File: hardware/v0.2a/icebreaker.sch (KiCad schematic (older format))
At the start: 108 parts, among them J1 Jumper, J10 Jumper, J11 Jumper, J12 Jumper, J13 Jumper, J14 Jumper, J15 Jumper, J16 Jumper, J17 Jumper, J18 Jumper, J19 Jumper, J2 Jumper, J20 Flash, J21 PMOD_1A, J22 PMOD_1B, J23 PMOD_2H, J24 PMOD_2P, J25 RGB Led, J26 5V AUX, J27 5V AUX, J3 Jumper, J4 Jumper, J5 Jumper, J6 Jumper, J7 Jumper, J8 Jumper, J9 Jumper, P1 pkl_USB_OTG, SW1 TACT, SW2 TACT, SW3 TACT, SW4 TACT, U1 93C46B-SOT-23-6, U2 3.3V, U3 1V2, U4 FT2232H, U5 W25Q, U6 ICE5LP4K-SG48, X1 12MHz

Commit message: Fixed #6 Oscillator pinout and schematic symbol.
Both bitsy and icebreaker.
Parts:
- removed X1: 12MHz, pkl_housings_sot:SOT-23-5, symbol pkl_device:Oscillator
- added U7: 12MHz, pkl_housings_sot:SOT-23-5, symbol pkl_device:pkl_oscillator_sit2001
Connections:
- wire segments 585 -> 581
- no-connect marks 17 -> 18
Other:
- moved on the sheet: C4, R7
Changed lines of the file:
@@
 $EndComp
 $Comp
-L pkl_device:Oscillator X1
-U 1 1 5A523EA3
-P 1900 6750
-F 0 "X1" H 1900 6355 60  0000 C CNN
-F 1 "12MHz" H 1900 6465 60  0000 C CNN
-F 2 "pkl_housings_sot:SOT-23-5" H 1900 6750 60  0001 C CNN
-F 3 "https://www.sitime.com/datasheet/SiT2001" H 1900 6750 60  0001 C CNN
-F 4 "12MHz Oscillator" H 1900 6750 50  0001 C CNN "Description"
-F 5 "SiTIME" H 1900 6750 50  0001 C CNN "Manufacturer"
-F 6 "SIT2001BI-S2-33E-12.000000G" H 1900 6750 50  0001 C CNN "MFN"
-F 7 "ANY" H 1900 6750 50  0001 C CNN "Source"
-F 8 "xtal-sot23-5-12mhz-osc" H 0   0   50  0001 C CNN "Key"
-	1    1900 6750
-	-1   0    0    1
-$EndComp
-Wire Wire Line
-	2300 6750 2400 6750
-$Comp
 L pkl_device:pkl_R_Small R7
 U 1 1 5A52417F
-P 2500 6750
-F 0 "R7" V 2550 6900 50  0000 C CNN
-F 1 "10k" V 2550 6600 50  0000 C CNN
-F 2 "pkl_dipol:R_0402" H 2559 6657 60  0001 L CNN
-F 3 "" H 2500 6750 60  0000 C CNN
-F 4 "ANY" H 2500 6750 50  0001 C CNN "Source"
-F 5 "res-0402-10k" H 0   0   50  0001 C CNN "Key"
-	1    2500 6750
-	0    1    1    0
+P 1300 6700
+F 0 "R7" V 1350 6850 50  0000 C CNN
+F 1 "10k" V 1350 6550 50  0000 C CNN
+F 2 "pkl_dipol:R_0402" H 1359 6607 60  0001 L CNN
+F 3 "" H 1300 6700 60  0000 C CNN
+F 4 "ANY" H 1300 6700 50  0001 C CNN "Source"
+F 5 "res-0402-10k" H -1200 -50 50  0001 C CNN "Key"
+	1    1300 6700
+	0    -1   -1   0
 $EndComp
 $Comp
 L power:+3V3 #PWR02
 U 1 1 5A524395
-P 2800 6550
-F 0 "#PWR02" H 2800 6400 50  0001 C CNN
-F 1 "+3V3" H 2815 6726 50  0000 C CNN
-F 2 "" H 2800 6550 50  0001 C CNN
-F 3 "" H 2800 6550 50  0001 C CNN
-	1    2800 6550
+P 1100 6600
+F 0 "#PWR02" H 1100 6450 50  0001 C CNN
+F 1 "+3V3" H 1115 6776 50  0000 C CNN
+F 2 "" H 1100 6600 50  0001 C CNN
+F 3 "" H 1100 6600 50  0001 C CNN
+	1    1100 6600
 	1    0    0    -1
 $EndComp
-Wire Wire Line
-	1500 6650 1400 6650
-Wire Wire Line
-	1400 6650 1400 6550
 $Comp
 L power:+3V3 #PWR03
 U 1 1 5A5243FF
-P 1400 6550
-F 0 "#PWR03" H 1400 6400 50  0001 C CNN
-F 1 "+3V3" H 1415 6726 50  0000 C CNN
-F 2 "" H 1400 6550 50  0001 C CNN
-F 3 "" H 1400 6550 50  0001 C CNN
-	1    1400 6550
+P 2600 6600
+F 0 "#PWR03" H 2600 6450 50  0001 C CNN
+F 1 "+3V3" H 2615 6776 50  0000 C CNN
+F 2 "" H 2600 6600 50  0001 C CNN
+F 3 "" H 2600 6600 50  0001 C CNN
+	1    2600 6600
 	1    0    0    -1
 $EndComp
-Wire Wire Line
-	1500 6750 1400 6750
-Wire Wire Line
-	1400 6750 1400 7050
 NoConn ~ 3100 6750
 Wire Wire Line
@@
 L pkl_device:pkl_C_Small C4
 U 1 1 5A526171
-P 1200 6850
-F 0 "C4" H 1292 6897 50  0000 L CNN
-F 1 "100n" H 1292 6804 50  0000 L CNN
-F 2 "pkl_dipol:C_0402" H 1292 6757 60  0001 L CNN
-F 3 "" H 1200 6850 60  0000 C CNN
-F 4 "ANY" H 1200 6850 50  0001 C CNN "Source"
-F 5 "cap-cer-0402-100n" H 0   0   50  0001 C CNN "Key"
-	1    1200 6850
-	-1   0    0    -1
+P 2600 7100
+F 0 "C4" H 2692 7147 50  0000 L CNN
+F 1 "100n" H 2692 7054 50  0000 L CNN
+F 2 "pkl_dipol:C_0402" H 2692 7007 60  0001 L CNN
+F 3 "" H 2600 7100 60  0000 C CNN
+F 4 "ANY" H 2600 7100 50  0001 C CNN "Source"
+F 5 "cap-cer-0402-100n" H 1400 250 50  0001 C CNN "Key"
+	1    2600 7100
+	1    0    0    -1
 $EndComp
-Wire Wire Line
-	1200 6950 1200 7050
-Wire Wire Line
-	1200 6750 1200 6650
-Wire Wire Line
-	1200 6650 1400 6650
-Connection ~ 1400 6650
 $Comp
 L power:GND #PWR05
 U 1 1 5A52451B
-P 1300 7150
-F 0 "#PWR05" H 1300 6900 50  0001 C CNN
-F 1 "GND" H 1305 6974 50  0000 C CNN
-F 2 "" H 1300 7150 50  0001 C CNN
-F 3 "" H 1300 7150 50  0001 C CNN
-	1    1300 7150
+P 1400 7300
+F 0 "#PWR05" H 1400 7050 50  0001 C CNN
+F 1 "GND" H 1405 7124 50  0000 C CNN
+F 2 "" H 1400 7300 50  0001 C CNN
+F 3 "" H 1400 7300 50  0001 C CNN
+	1    1400 7300
 	1    0    0    -1
 $EndComp
-Wire Wire Line
-	1200 7050 1300 7050
-Wire Wire Line
-	1300 7050 1300 7150
-Connection ~ 1300 7050
-Wire Wire Line
-	1300 7050 1400 7050
-Wire Wire Line
-	2600 6750 2800 6750
-Wire Wire Line
-	2800 6550 2800 6750
-Text Notes 2300 6950 0    50   ~ 0
+Text Notes 1000 6850 0    50   ~ 0
 10k or less
 $Comp
@@
 	5300 1750 5300 1850
 Wire Wire Line
-	2300 6650 3000 6650
+	2500 6900 2800 6900
 Wire Wire Line
-	3000 6650 3000 6350
+	2800 6900 2800 6350
 Wire Wire Line
-	3000 6350 3100 6350
+	2800 6350 3100 6350
 $Comp
 L pkl_memory:93C46-SOT-23-6 U1
@@
 Wire Notes Line
 	11600 9900 7000 9900
-Text Label 2400 6650 0    50   ~ 0
+Text Label 3050 6350 2    50   ~ 0
 FTDI_CLK
 Text Label 10800 3400 0    50   ~ 0
@@
 Wire Wire Line
 	15200 8700 15600 8700
+$Comp
+L pkl_device:pkl_oscillator_sit2001 U7
+U 1 1 5AACB5B6
+P 2000 6800
+F 0 "U7" H 2000 7170 50  0000 C CNN
+F 1 "12MHz" H 2000 7077 50  0000 C CNN
+F 2 "pkl_housings_sot:SOT-23-5" H 2000 6700 50  0001 C CNN
+F 3 "" H 2000 6700 50  0001 C CNN
+F 4 "ANY" H 2000 6800 50  0001 C CNN "Source"
+	1    2000 6800
+	-1   0    0    -1
+$EndComp
+Wire Wire Line
+	2500 6700 2600 6700
+Wire Wire Line
+	2600 6700 2600 6600
+Wire Wire Line
+	1500 6700 1400 6700
+Wire Wire Line
+	1200 6700 1100 6700
+Wire Wire Line
+	1100 6700 1100 6600
+Wire Wire Line
+	2600 6700 2600 7000
+Connection ~ 2600 6700
+Wire Wire Line
+	2600 7200 2600 7300
+$Comp
+L power:GND #PWR0101
+U 1 1 5B00D06C
+P 2600 7300
+F 0 "#PWR0101" H 2600 7050 50  0001 C CNN
+F 1 "GND" H 2605 7124 50  0000 C CNN
+F 2 "" H 2600 7300 50  0001 C CNN
+F 3 "" H 2600 7300 50  0001 C CNN
+	1    2600 7300
+	1    0    0    -1
+$EndComp
+Wire Wire Line
+	1500 6900 1400 6900
+Wire Wire Line
+	1400 6900 1400 7300
+NoConn ~ 1500 6800
 $EndSCHEMATC

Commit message: Replaced 0402 4.7u capacitors with 0603 for consistency. Fixes #4
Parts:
- C6, C7, C9: footprint pkl_dipol:C_0402 -> pkl_dipol:C_0603; symbol pkl_device:pkl_C_Small -> pkl_device:pkl_C
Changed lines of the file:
@@
 $EndComp
 $Comp
-L pkl_device:pkl_C_Small C9
+L pkl_device:pkl_C C9
 U 1 1 5A54C880
 P 3000 2450
 F 0 "C9" H 3100 2550 50  0000 L CNN
 F 1 "4u7" H 3050 2350 50  0000 L CNN
-F 2 "pkl_dipol:C_0402" H 3092 2357 60  0001 L CNN
+F 2 "pkl_dipol:C_0603" H 3092 2357 60  0001 L CNN
 F 3 "" H 3000 2450 60  0000 C CNN
-F 4 "ANY" H 3000 2450 50  0001 C CNN "Source"
-F 5 "cap-cer-0402-4u7" H 0   0   50  0001 C CNN "Key"
+F 4 "cap-cer-0402-4u7" H 0   0   50  0001 C CNN "Key"
+F 5 "ANY" H 3000 2450 50  0001 C CNN "Source"
 	1    3000 2450
 	-1   0    0    -1
 $EndComp
 $Comp
-L pkl_device:pkl_C_Small C6
+L pkl_device:pkl_C C6
 U 1 1 5A54CA7C
 P 2700 2450
 F 0 "C6" H 2800 2550 50  0000 L CNN
 F 1 "4u7" H 2750 2350 50  0000 L CNN
-F 2 "pkl_dipol:C_0402" H 2792 2357 60  0001 L CNN
+F 2 "pkl_dipol:C_0603" H 2792 2357 60  0001 L CNN
 F 3 "" H 2700 2450 60  0000 C CNN
-F 4 "ANY" H 2700 2450 50  0001 C CNN "Source"
-F 5 "cap-cer-0402-4u7" H 0   0   50  0001 C CNN "Key"
+F 4 "cap-cer-0402-4u7" H 0   0   50  0001 C CNN "Key"
+F 5 "ANY" H 2700 2450 50  0001 C CNN "Source"
 	1    2700 2450
 	-1   0    0    -1
@@
 	10950 8250 11050 8250
 $Comp
-L pkl_device:pkl_C_Small C7
+L pkl_device:pkl_C C7
 U 1 1 5A57F2C5
 P 2700 3650
 F 0 "C7" H 2815 3697 50  0000 L CNN
 F 1 "4u7" H 2815 3604 50  0000 L CNN
-F 2 "pkl_dipol:C_0402" H 2792 3557 60  0001 L CNN
+F 2 "pkl_dipol:C_0603" H 2792 3557 60  0001 L CNN
 F 3 "" H 2700 3650 60  0000 C CNN
-F 4 "ANY" H 2700 3650 50  0001 C CNN "Source"
-F 5 "cap-cer-0402-4u7" H 0   0   50  0001 C CNN "Key"
+F 4 "cap-cer-0402-4u7" H 0   0   50  0001 C CNN "Key"
+F 5 "ANY" H 2700 3650 50  0001 C CNN "Source"
 	1    2700 3650
 	-1   0    0    -1

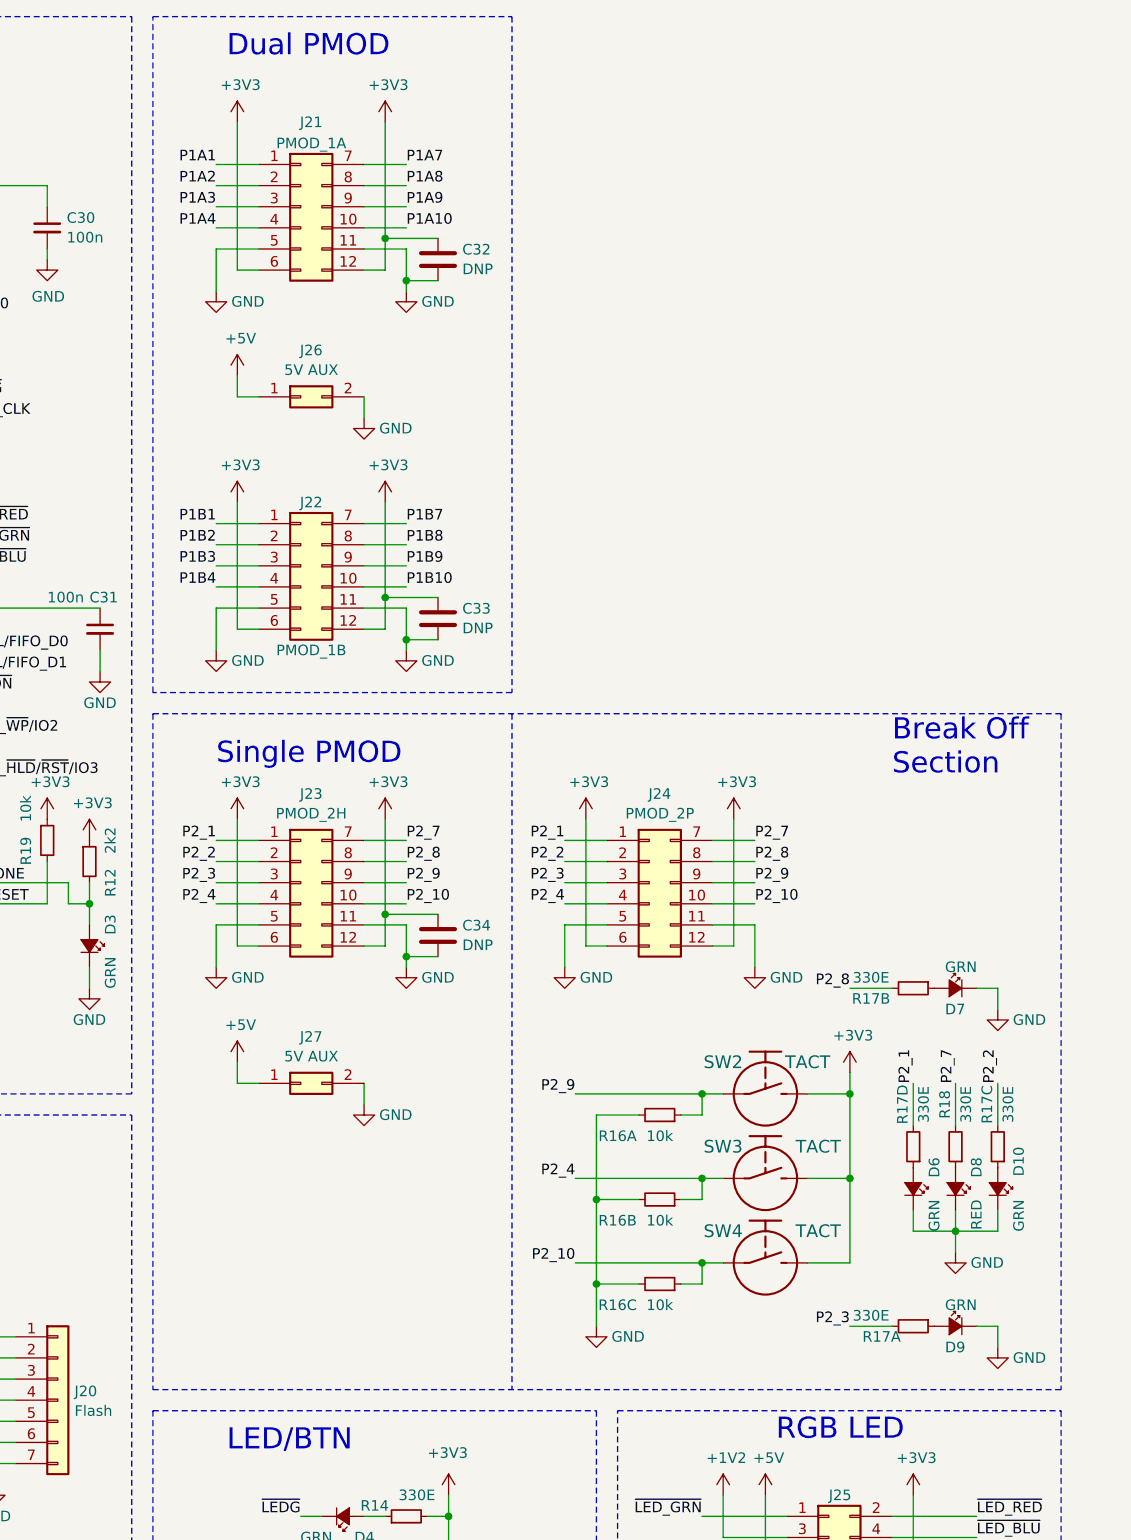
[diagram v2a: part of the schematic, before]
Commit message: Added inline resistors on all PMOD connectors to allow for higher GPIO speeds.
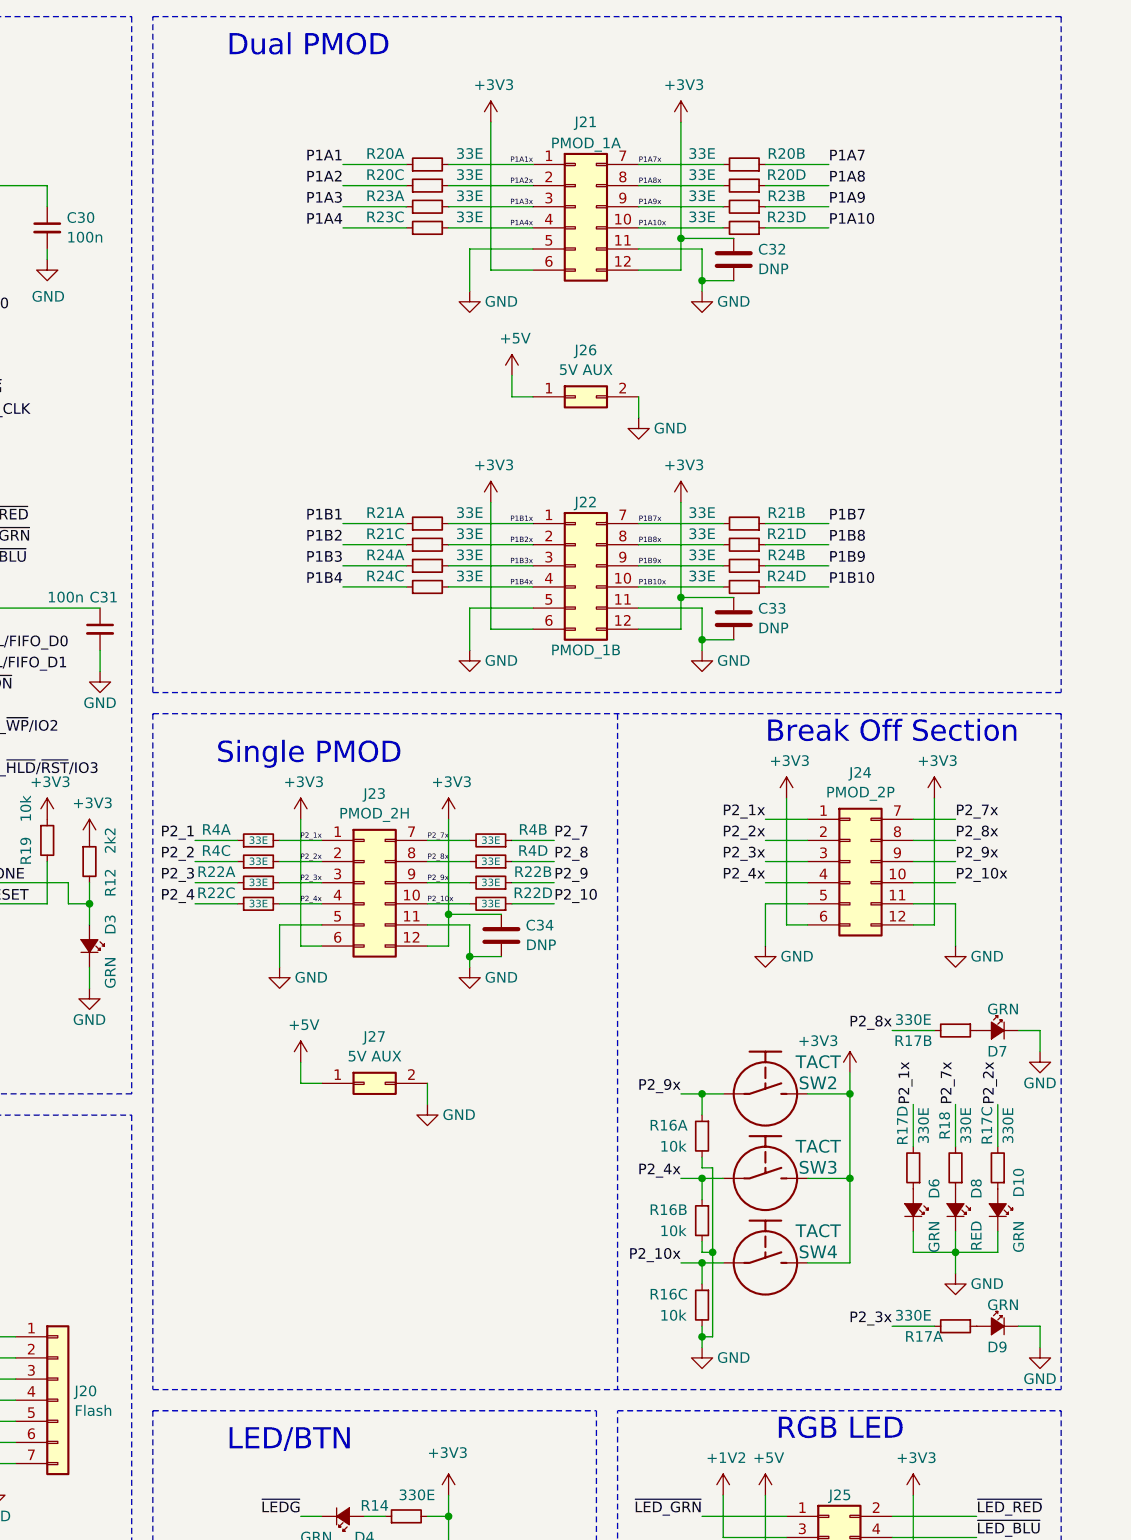
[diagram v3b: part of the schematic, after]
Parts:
- added R20, R21, R22, R23, R24, R4: 33E, pkl_dipol:R_Array_Convex_4x0402, symbol pkl_device:pkl_R4_Small
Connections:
- net P1A1: now also R20.1; no longer J21.1 (Pin_1)
- net P1A10: now also R23.7; no longer J21.10 (Pin_10)
- net P1A2: now also R20.5; no longer J21.2 (Pin_2)
- net P1A3: now also R23.1; no longer J21.3 (Pin_3)
- net P1A4: now also R23.5; no longer J21.4 (Pin_4)
- net P1A7: now also R20.3; no longer J21.7 (Pin_7)
- net P1A8: now also R20.7; no longer J21.8 (Pin_8)
- net P1A9: now also R23.3; no longer J21.9 (Pin_9)
- net P1B1: now also R21.1; no longer J22.1 (Pin_1)
- net P1B10: now also R24.7; no longer J22.10 (Pin_10)
- net P1B2: now also R21.5; no longer J22.2 (Pin_2)
- net P1B3: now also R24.1; no longer J22.3 (Pin_3)
- net P1B4: now also R24.5; no longer J22.4 (Pin_4)
- net P1B7: now also R21.3; no longer J22.7 (Pin_7)
- net P1B8: now also R21.7; no longer J22.8 (Pin_8)
- net P1B9: now also R24.3; no longer J22.9 (Pin_9)
- net P2_1: now also R4.1; no longer J23.1 (Pin_1), J24.1 (Pin_1), R17.8
- net P2_10: now also R22.7; no longer J23.10 (Pin_10), J24.10 (Pin_10), R16.5, SW4.1
- net P2_2: now also R4.5; no longer J23.2 (Pin_2), J24.2 (Pin_2), R17.6
- net P2_3: now also R22.1; no longer J23.3 (Pin_3), J24.3 (Pin_3), R17.2
- net P2_4: now also R22.5; no longer J23.4 (Pin_4), J24.4 (Pin_4), R16.3, SW3.1
- net P2_7: now also R4.3; no longer J23.7 (Pin_7), J24.7 (Pin_7), R18.2
- net P2_8: now also R4.7; no longer J23.8 (Pin_8), J24.8 (Pin_8), R17.4
- net P2_9: now also R22.3; no longer J23.9 (Pin_9), J24.9 (Pin_9), R16.1, SW2.1
- new net P1A10x: J21.10 (Pin_10), R23.8
- new net P1A1x: J21.1 (Pin_1), R20.2
- new net P1A2x: J21.2 (Pin_2), R20.6
- new net P1A3x: J21.3 (Pin_3), R23.2
- new net P1A4x: J21.4 (Pin_4), R23.6
- new net P1A7x: J21.7 (Pin_7), R20.4
- new net P1A8x: J21.8 (Pin_8), R20.8
- new net P1A9x: J21.9 (Pin_9), R23.4
- new net P1B10x: J22.10 (Pin_10), R24.8
- new net P1B1x: J22.1 (Pin_1), R21.2
- new net P1B2x: J22.2 (Pin_2), R21.6
- new net P1B3x: J22.3 (Pin_3), R24.2
- new net P1B4x: J22.4 (Pin_4), R24.6
- new net P1B7x: J22.7 (Pin_7), R21.4
- new net P1B8x: J22.8 (Pin_8), R21.8
- new net P1B9x: J22.9 (Pin_9), R24.4
- new net P2_10x: J23.10 (Pin_10), J24.10 (Pin_10), R16.5, R22.8, SW4.1
- new net P2_1x: J23.1 (Pin_1), J24.1 (Pin_1), R17.8, R4.2
- new net P2_2x: J23.2 (Pin_2), J24.2 (Pin_2), R17.6, R4.6
- new net P2_3x: J23.3 (Pin_3), J24.3 (Pin_3), R17.2, R22.2
- new net P2_4x: J23.4 (Pin_4), J24.4 (Pin_4), R16.3, R22.6, SW3.1
- new net P2_7x: J23.7 (Pin_7), J24.7 (Pin_7), R18.2, R4.4
- new net P2_8x: J23.8 (Pin_8), J24.8 (Pin_8), R17.4, R4.8
- new net P2_9x: J23.9 (Pin_9), J24.9 (Pin_9), R16.1, R22.4, SW2.1
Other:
- note added: "Break Off Section"
- note removed: "Break Off\nSection"
- moved on the sheet: C32, C33, C34, D10, D6, D7, D8, D9, J21, J22, J23, J24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
